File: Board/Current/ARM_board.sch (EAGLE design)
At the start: 173 parts, among them IC3 STM32F437VI, IC4 LM358DT, J1 USART/I2C, J10 ANALOG, J11 DGND, J12 DPWR, J13 DIGITAL, J14 SGND, J15 SPWR, J16 SERVO, J2 I2C2/USART3, J3 USART2, J5 SPI, J6 Bluesmirf, J7 SWD, J8 AGND, J9 APWR, Q1 STL4P2UH7, Q2 2STR1230, Q3 STL4P2UH7, SW1 SW, U1 LSM330, U10 BAV99, U11 BAV99, U12 USBLC6-2, U13 USBLC6-2, U14 STMPS2171MTR, U15 MC74HC164, U3 NC7SZU04, U4 L6206Q, U5 L6206Q, U6 SI7617, U7 SI7617, U8 SI7617, U9 SI7617, Y2 8MHz

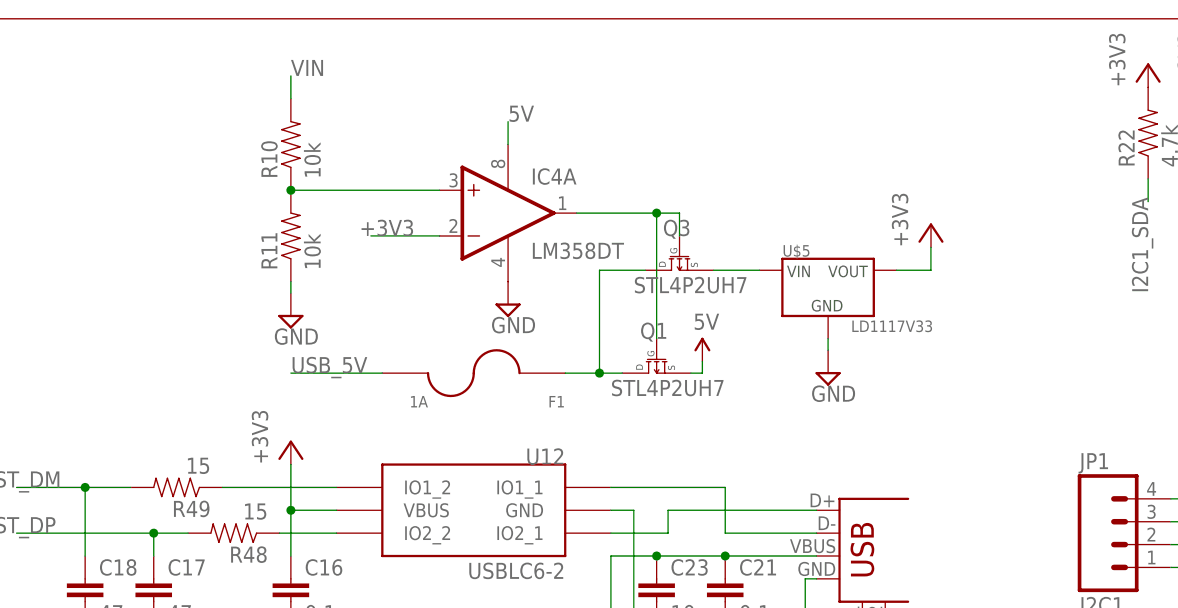
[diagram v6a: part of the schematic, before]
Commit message: Completed layout of new USB power parts.
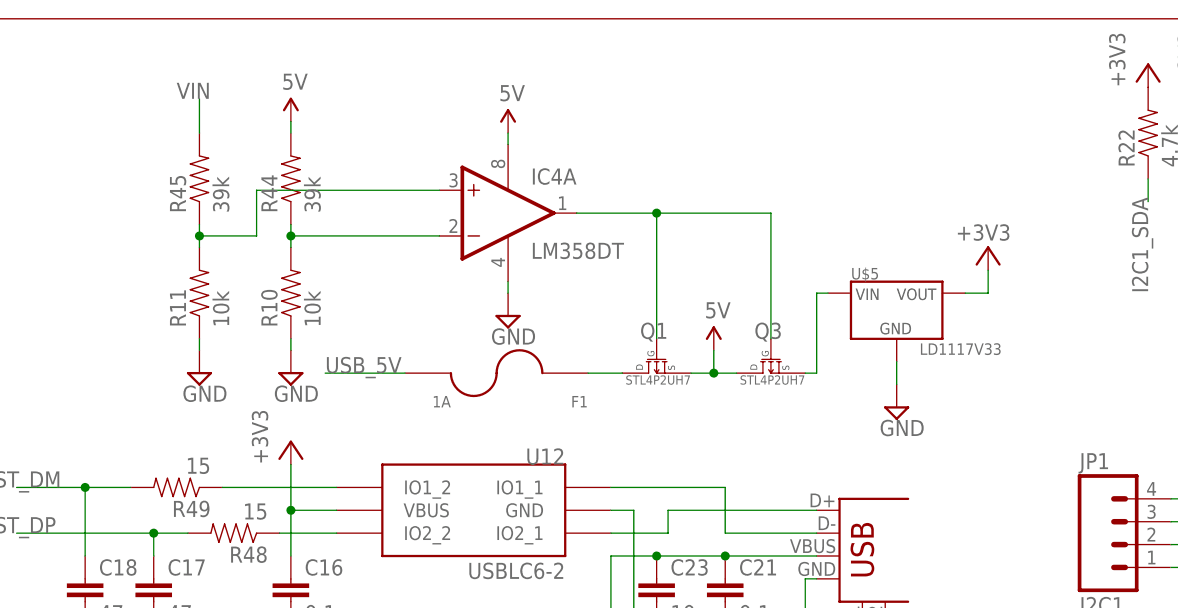
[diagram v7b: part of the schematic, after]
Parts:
- added R44, R45: 39k, SparkFun:RESISTOR0402-RES
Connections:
- removed net N$15: F1.1, Q1.D, Q3.D
- new net N$32: F1.1, Q1.D
- new net N$35: IC4A.-IN, R10.2, R44.1
- net +3V3: no longer IC4A.-IN
- net 5V: now also Q3.D, R44.2
- net GND: now also R10.1
- net N$5: now also R45.1; no longer R10.1
- net VIN: now also R45.2; no longer R10.2
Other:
- moved on the sheet: F1, Q3, R10, R11, U$5

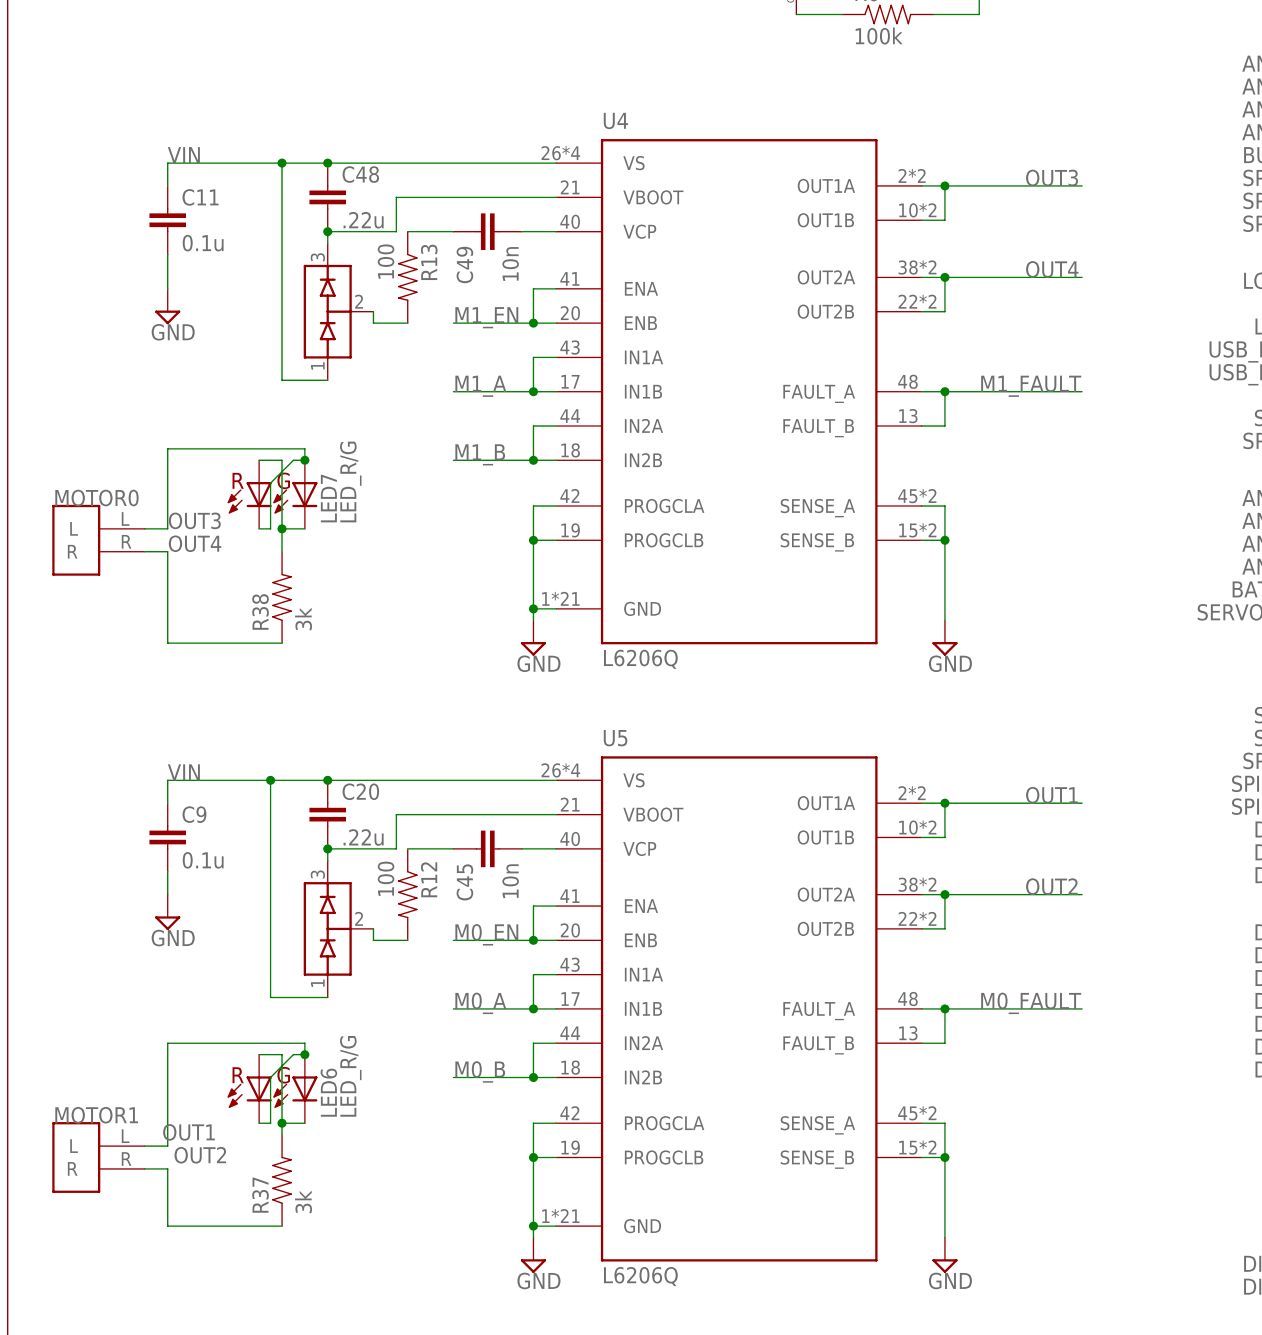
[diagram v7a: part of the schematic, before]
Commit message: Fixed the motor pins being swapped. Re-did a lot of the layout by the motors. Changed the big power traces that go through the center of the board to polygons.
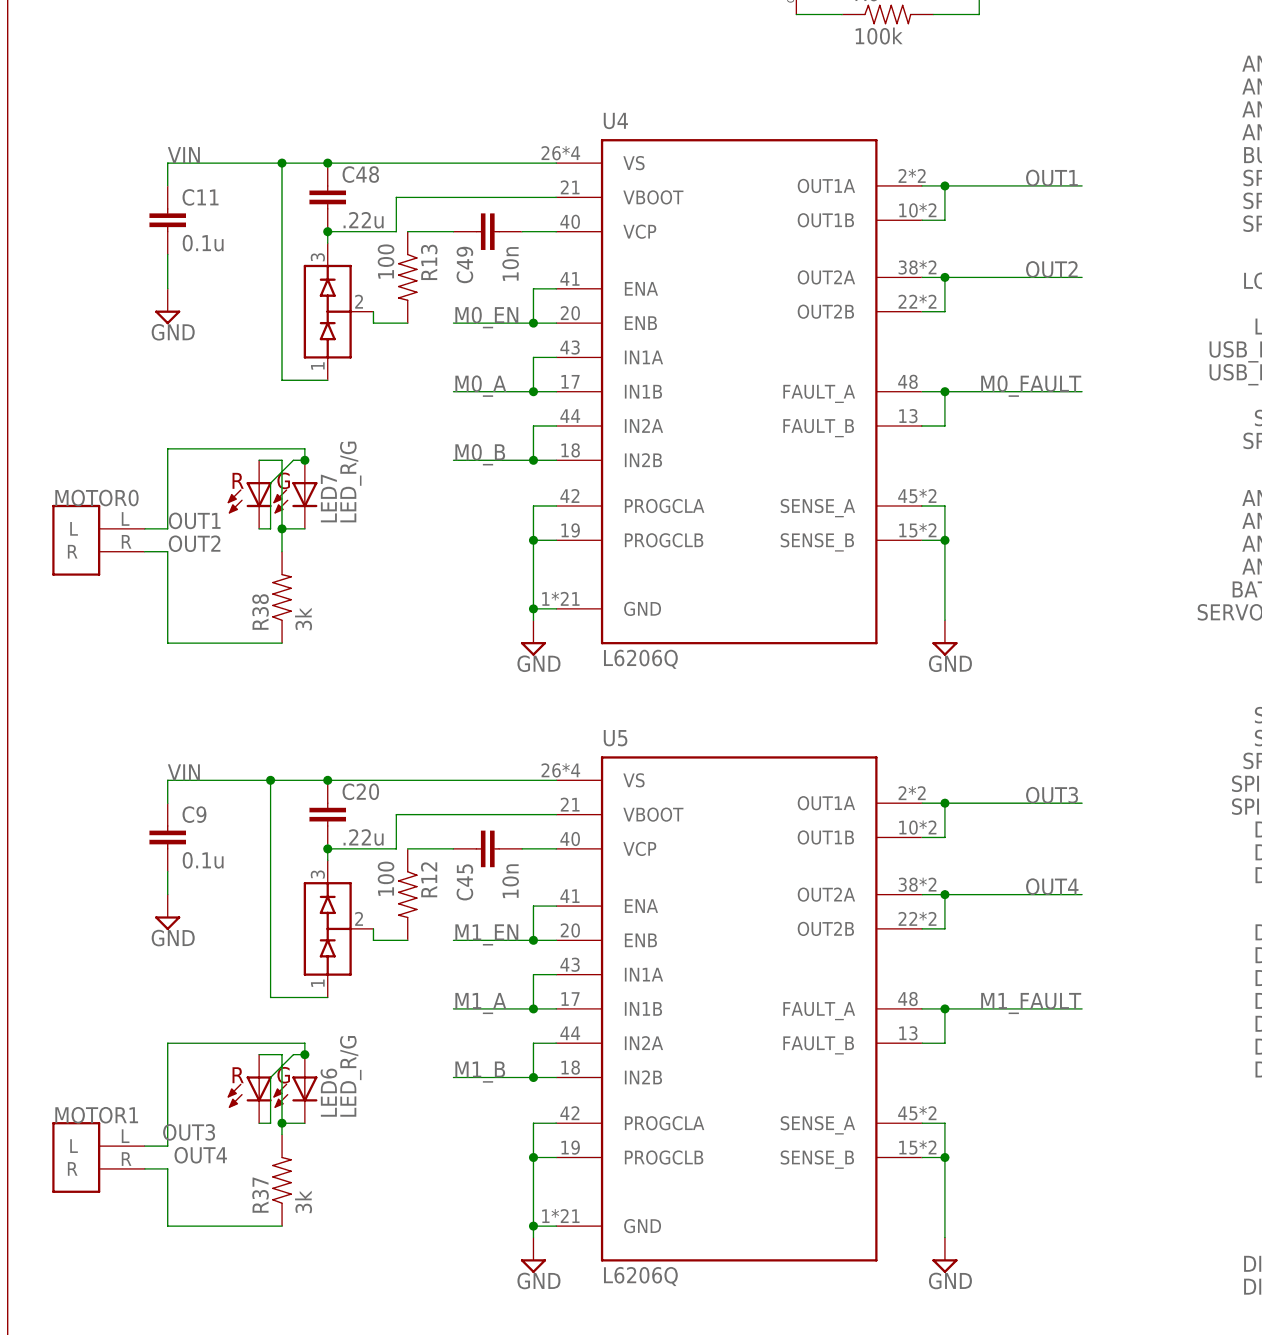
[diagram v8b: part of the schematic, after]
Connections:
- net M0_A: now also U4.IN1A, U4.IN1B; no longer U5.IN1A, U5.IN1B
- net M0_B: now also U4.IN2A, U4.IN2B; no longer U5.IN2A, U5.IN2B
- net M0_EN: now also U4.ENA, U4.ENB; no longer U5.ENA, U5.ENB
- net M0_FAULT: now also U4.FAULT_A, U4.FAULT_B; no longer U5.FAULT_A, U5.FAULT_B
- net M1_A: now also U5.IN1A, U5.IN1B; no longer U4.IN1A, U4.IN1B
- net M1_B: now also U5.IN2A, U5.IN2B; no longer U4.IN2A, U4.IN2B
- net M1_EN: now also U5.ENA, U5.ENB; no longer U4.ENA, U4.ENB
- net M1_FAULT: now also U5.FAULT_A, U5.FAULT_B; no longer U4.FAULT_A, U4.FAULT_B
- net OUT1: now also LED7.2, LED7.3, MOTOR0.L, U4.OUT1A, U4.OUT1B; no longer LED6.2, LED6.3, MOTOR1.L, U5.OUT1A, U5.OUT1B
- net OUT2: now also MOTOR0.R, R38.1, U4.OUT2A, U4.OUT2B; no longer MOTOR1.R, R37.1, U5.OUT2A, U5.OUT2B
- net OUT3: now also LED6.2, LED6.3, MOTOR1.L, U5.OUT1A, U5.OUT1B; no longer LED7.2, LED7.3, MOTOR0.L, U4.OUT1A, U4.OUT1B
- net OUT4: now also MOTOR1.R, R37.1, U5.OUT2A, U5.OUT2B; no longer MOTOR0.R, R38.1, U4.OUT2A, U4.OUT2B
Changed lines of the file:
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@@
 <setting verticaltext="up"/>
 </settings>
-<grid distance="0.05" unitdist="inch" unit="inch" style="lines" multiple="1" display="no" altdistance="0.01" altunitdist="inch" altunit="inch"/>
+<grid distance="0.1" unitdist="inch" unit="inch" style="lines" multiple="1" display="no" altdistance="0.01" altunitdist="inch" altunit="inch"/>
 <layers>
 <layer number="1" name="Top" color="4" fill="1" visible="no" active="no"/>
@@
 </segment>
 </net>
-<net name="OUT1" class="0">
+<net name="OUT3" class="0">
 <segment>
 <wire x1="15.24" y1="30.48" x2="17.78" y2="30.48" width="0.1524" layer="91"/>
@@
 </segment>
 </net>
-<net name="OUT2" class="0">
+<net name="OUT4" class="0">
 <segment>
 <wire x1="15.24" y1="27.94" x2="17.78" y2="27.94" width="0.1524" layer="91"/>
@@
 </segment>
 </net>
-<net name="OUT3" class="0">
+<net name="OUT1" class="0">
 <segment>
 <wire x1="15.24" y1="99.06" x2="17.78" y2="99.06" width="0.1524" layer="91"/>
@@
 </segment>
 </net>
-<net name="OUT4" class="0">
+<net name="OUT2" class="0">
 <segment>
 <wire x1="15.24" y1="96.52" x2="17.78" y2="96.52" width="0.1524" layer="91"/>
@@
 </segment>
 <segment>
-<pinref part="U5" gate="G$1" pin="IN1B"/>
-<wire x1="60.96" y1="45.72" x2="58.42" y2="45.72" width="0.1524" layer="91"/>
-<label x="49.53" y="45.72" size="1.778" layer="95"/>
-<pinref part="U5" gate="G$1" pin="IN1A"/>
-<wire x1="58.42" y1="45.72" x2="49.53" y2="45.72" width="0.1524" layer="91"/>
-<wire x1="60.96" y1="49.53" x2="58.42" y2="49.53" width="0.1524" layer="91"/>
-<wire x1="58.42" y1="49.53" x2="58.42" y2="45.72" width="0.1524" layer="91"/>
-<junction x="58.42" y="45.72"/>
+<pinref part="U4" gate="G$1" pin="IN1B"/>
+<wire x1="60.96" y1="114.3" x2="58.42" y2="114.3" width="0.1524" layer="91"/>
+<label x="49.53" y="114.3" size="1.778" layer="95"/>
+<pinref part="U4" gate="G$1" pin="IN1A"/>
+<wire x1="58.42" y1="114.3" x2="49.53" y2="114.3" width="0.1524" layer="91"/>
+<wire x1="60.96" y1="118.11" x2="58.42" y2="118.11" width="0.1524" layer="91"/>
+<wire x1="58.42" y1="118.11" x2="58.42" y2="114.3" width="0.1524" layer="91"/>
+<junction x="58.42" y="114.3"/>
 </segment>
 </net>
@@
 </segment>
 <segment>
-<pinref part="U5" gate="G$1" pin="IN2B"/>
-<wire x1="60.96" y1="38.1" x2="58.42" y2="38.1" width="0.1524" layer="91"/>
-<label x="49.53" y="38.1" size="1.778" layer="95"/>
-<pinref part="U5" gate="G$1" pin="IN2A"/>
-<wire x1="58.42" y1="38.1" x2="49.53" y2="38.1" width="0.1524" layer="91"/>
-<wire x1="60.96" y1="41.91" x2="58.42" y2="41.91" width="0.1524" layer="91"/>
-<wire x1="58.42" y1="41.91" x2="58.42" y2="38.1" width="0.1524" layer="91"/>
-<junction x="58.42" y="38.1"/>
+<pinref part="U4" gate="G$1" pin="IN2B"/>
+<wire x1="60.96" y1="106.68" x2="58.42" y2="106.68" width="0.1524" layer="91"/>
+<label x="49.53" y="106.68" size="1.778" layer="95"/>
+<pinref part="U4" gate="G$1" pin="IN2A"/>
+<wire x1="58.42" y1="106.68" x2="49.53" y2="106.68" width="0.1524" layer="91"/>
+<wire x1="60.96" y1="110.49" x2="58.42" y2="110.49" width="0.1524" layer="91"/>
+<wire x1="58.42" y1="110.49" x2="58.42" y2="106.68" width="0.1524" layer="91"/>
+<junction x="58.42" y="106.68"/>
 </segment>
 </net>
@@
 </segment>
 <segment>
-<pinref part="U5" gate="G$1" pin="ENB"/>
-<wire x1="60.96" y1="53.34" x2="58.42" y2="53.34" width="0.1524" layer="91"/>
-<label x="49.53" y="53.34" size="1.778" layer="95"/>
-<pinref part="U5" gate="G$1" pin="ENA"/>
-<wire x1="58.42" y1="53.34" x2="49.53" y2="53.34" width="0.1524" layer="91"/>
-<wire x1="60.96" y1="57.15" x2="58.42" y2="57.15" width="0.1524" layer="91"/>
-<wire x1="58.42" y1="57.15" x2="58.42" y2="53.34" width="0.1524" layer="91"/>
-<junction x="58.42" y="53.34"/>
+<pinref part="U4" gate="G$1" pin="ENB"/>
+<wire x1="60.96" y1="121.92" x2="58.42" y2="121.92" width="0.1524" layer="91"/>
+<label x="49.53" y="121.92" size="1.778" layer="95"/>
+<pinref part="U4" gate="G$1" pin="ENA"/>
+<wire x1="58.42" y1="121.92" x2="49.53" y2="121.92" width="0.1524" layer="91"/>
+<wire x1="60.96" y1="125.73" x2="58.42" y2="125.73" width="0.1524" layer="91"/>
+<wire x1="58.42" y1="125.73" x2="58.42" y2="121.92" width="0.1524" layer="91"/>
+<junction x="58.42" y="121.92"/>
 </segment>
 </net>
@@
 </segment>
 <segment>
-<pinref part="U4" gate="G$1" pin="IN1B"/>
-<wire x1="60.96" y1="114.3" x2="58.42" y2="114.3" width="0.1524" layer="91"/>
-<label x="49.53" y="114.3" size="1.778" layer="95"/>
-<pinref part="U4" gate="G$1" pin="IN1A"/>
-<wire x1="58.42" y1="114.3" x2="49.53" y2="114.3" width="0.1524" layer="91"/>
-<wire x1="60.96" y1="118.11" x2="58.42" y2="118.11" width="0.1524" layer="91"/>
-<wire x1="58.42" y1="118.11" x2="58.42" y2="114.3" width="0.1524" layer="91"/>
-<junction x="58.42" y="114.3"/>
+<pinref part="U5" gate="G$1" pin="IN1B"/>
+<wire x1="60.96" y1="45.72" x2="58.42" y2="45.72" width="0.1524" layer="91"/>
+<label x="49.53" y="45.72" size="1.778" layer="95"/>
+<pinref part="U5" gate="G$1" pin="IN1A"/>
+<wire x1="58.42" y1="45.72" x2="49.53" y2="45.72" width="0.1524" layer="91"/>
+<wire x1="60.96" y1="49.53" x2="58.42" y2="49.53" width="0.1524" layer="91"/>
+<wire x1="58.42" y1="49.53" x2="58.42" y2="45.72" width="0.1524" layer="91"/>
+<junction x="58.42" y="45.72"/>
 </segment>
 </net>
@@
 </segment>
 <segment>
-<pinref part="U4" gate="G$1" pin="ENB"/>
-<wire x1="60.96" y1="121.92" x2="58.42" y2="121.92" width="0.1524" layer="91"/>
-<label x="49.53" y="121.92" size="1.778" layer="95"/>
-<pinref part="U4" gate="G$1" pin="ENA"/>
-<wire x1="58.42" y1="121.92" x2="49.53" y2="121.92" width="0.1524" layer="91"/>
-<wire x1="60.96" y1="125.73" x2="58.42" y2="125.73" width="0.1524" layer="91"/>
-<wire x1="58.42" y1="125.73" x2="58.42" y2="121.92" width="0.1524" layer="91"/>
-<junction x="58.42" y="121.92"/>
+<pinref part="U5" gate="G$1" pin="ENB"/>
+<wire x1="60.96" y1="53.34" x2="58.42" y2="53.34" width="0.1524" layer="91"/>
+<label x="49.53" y="53.34" size="1.778" layer="95"/>
+<pinref part="U5" gate="G$1" pin="ENA"/>
+<wire x1="58.42" y1="53.34" x2="49.53" y2="53.34" width="0.1524" layer="91"/>
+<wire x1="60.96" y1="57.15" x2="58.42" y2="57.15" width="0.1524" layer="91"/>
+<wire x1="58.42" y1="57.15" x2="58.42" y2="53.34" width="0.1524" layer="91"/>
+<junction x="58.42" y="53.34"/>
 </segment>
 </net>
@@
 </segment>
 <segment>
-<pinref part="U4" gate="G$1" pin="IN2B"/>
-<wire x1="60.96" y1="106.68" x2="58.42" y2="106.68" width="0.1524" layer="91"/>
-<label x="49.53" y="106.68" size="1.778" layer="95"/>
-<pinref part="U4" gate="G$1" pin="IN2A"/>
-<wire x1="58.42" y1="106.68" x2="49.53" y2="106.68" width="0.1524" layer="91"/>
-<wire x1="60.96" y1="110.49" x2="58.42" y2="110.49" width="0.1524" layer="91"/>
-<wire x1="58.42" y1="110.49" x2="58.42" y2="106.68" width="0.1524" layer="91"/>
-<junction x="58.42" y="106.68"/>
+<pinref part="U5" gate="G$1" pin="IN2B"/>
+<wire x1="60.96" y1="38.1" x2="58.42" y2="38.1" width="0.1524" layer="91"/>
+<label x="49.53" y="38.1" size="1.778" layer="95"/>
+<pinref part="U5" gate="G$1" pin="IN2A"/>
+<wire x1="58.42" y1="38.1" x2="49.53" y2="38.1" width="0.1524" layer="91"/>
+<wire x1="60.96" y1="41.91" x2="58.42" y2="41.91" width="0.1524" layer="91"/>
+<wire x1="58.42" y1="41.91" x2="58.42" y2="38.1" width="0.1524" layer="91"/>
+<junction x="58.42" y="38.1"/>
 </segment>
 </net>
@@
 </segment>
 <segment>
-<pinref part="U5" gate="G$1" pin="FAULT_A"/>
-<wire x1="101.6" y1="45.72" x2="104.14" y2="45.72" width="0.1524" layer="91"/>
-<wire x1="104.14" y1="45.72" x2="119.38" y2="45.72" width="0.1524" layer="91"/>
-<pinref part="U5" gate="G$1" pin="FAULT_B"/>
-<wire x1="101.6" y1="41.91" x2="104.14" y2="41.91" width="0.1524" layer="91"/>
-<wire x1="104.14" y1="41.91" x2="104.14" y2="45.72" width="0.1524" layer="91"/>
-<junction x="104.14" y="45.72"/>
-<label x="107.95" y="45.72" size="1.778" layer="95"/>
+<pinref part="U4" gate="G$1" pin="FAULT_A"/>
+<wire x1="101.6" y1="114.3" x2="104.14" y2="114.3" width="0.1524" layer="91"/>
+<wire x1="104.14" y1="114.3" x2="119.38" y2="114.3" width="0.1524" layer="91"/>
+<pinref part="U4" gate="G$1" pin="FAULT_B"/>
+<wire x1="101.6" y1="110.49" x2="104.14" y2="110.49" width="0.1524" layer="91"/>
+<wire x1="104.14" y1="110.49" x2="104.14" y2="114.3" width="0.1524" layer="91"/>
+<junction x="104.14" y="114.3"/>
+<label x="107.95" y="114.3" size="1.778" layer="95"/>
 </segment>
 </net>
@@
 </segment>
 <segment>
-<pinref part="U4" gate="G$1" pin="FAULT_A"/>
-<wire x1="101.6" y1="114.3" x2="104.14" y2="114.3" width="0.1524" layer="91"/>
-<wire x1="104.14" y1="114.3" x2="119.38" y2="114.3" width="0.1524" layer="91"/>
-<pinref part="U4" gate="G$1" pin="FAULT_B"/>
-<wire x1="101.6" y1="110.49" x2="104.14" y2="110.49" width="0.1524" layer="91"/>
-<wire x1="104.14" y1="110.49" x2="104.14" y2="114.3" width="0.1524" layer="91"/>
-<junction x="104.14" y="114.3"/>
-<label x="107.95" y="114.3" size="1.778" layer="95"/>
+<pinref part="U5" gate="G$1" pin="FAULT_A"/>
+<wire x1="101.6" y1="45.72" x2="104.14" y2="45.72" width="0.1524" layer="91"/>
+<wire x1="104.14" y1="45.72" x2="119.38" y2="45.72" width="0.1524" layer="91"/>
+<pinref part="U5" gate="G$1" pin="FAULT_B"/>
+<wire x1="101.6" y1="41.91" x2="104.14" y2="41.91" width="0.1524" layer="91"/>
+<wire x1="104.14" y1="41.91" x2="104.14" y2="45.72" width="0.1524" layer="91"/>
+<junction x="104.14" y="45.72"/>
+<label x="107.95" y="45.72" size="1.778" layer="95"/>
 </segment>
 </net>
